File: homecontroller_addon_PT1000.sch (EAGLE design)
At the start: 46 parts, among them U1 OPA2188AIDGKR, U2 OPA2188AIDGKR, U3 REF3025AIDBZTG4, U4 ADS1015IDGST, X1 S2L3.50/10/90G

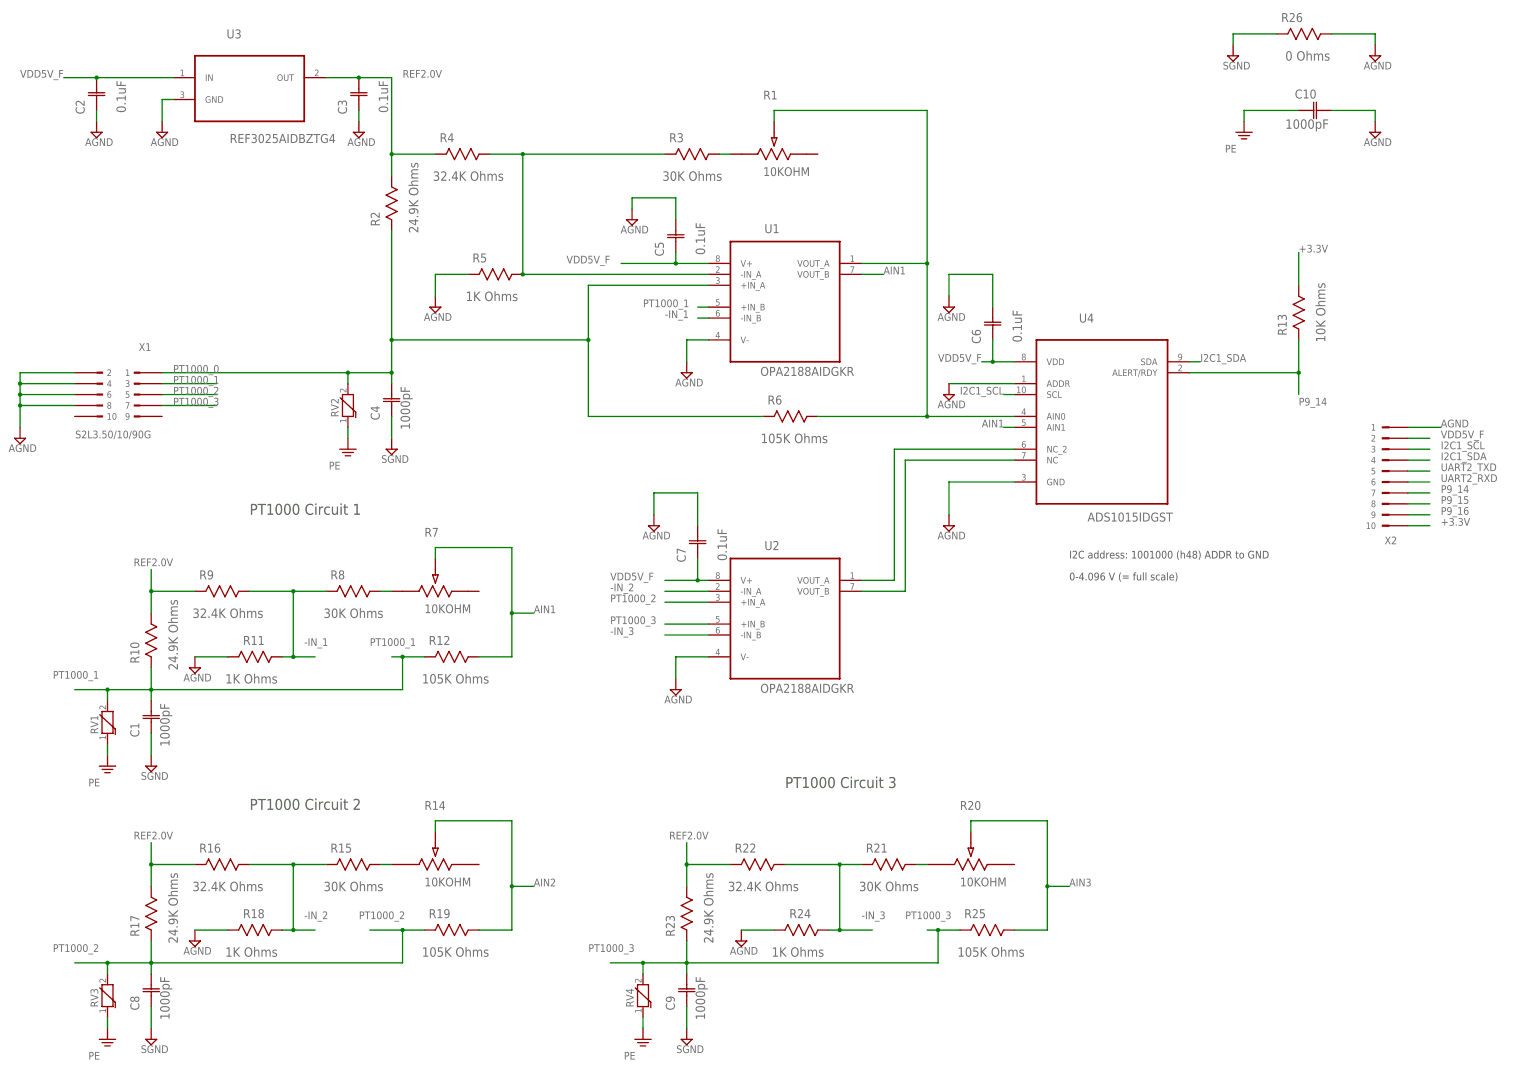
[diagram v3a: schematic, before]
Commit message: optimisation of BOM
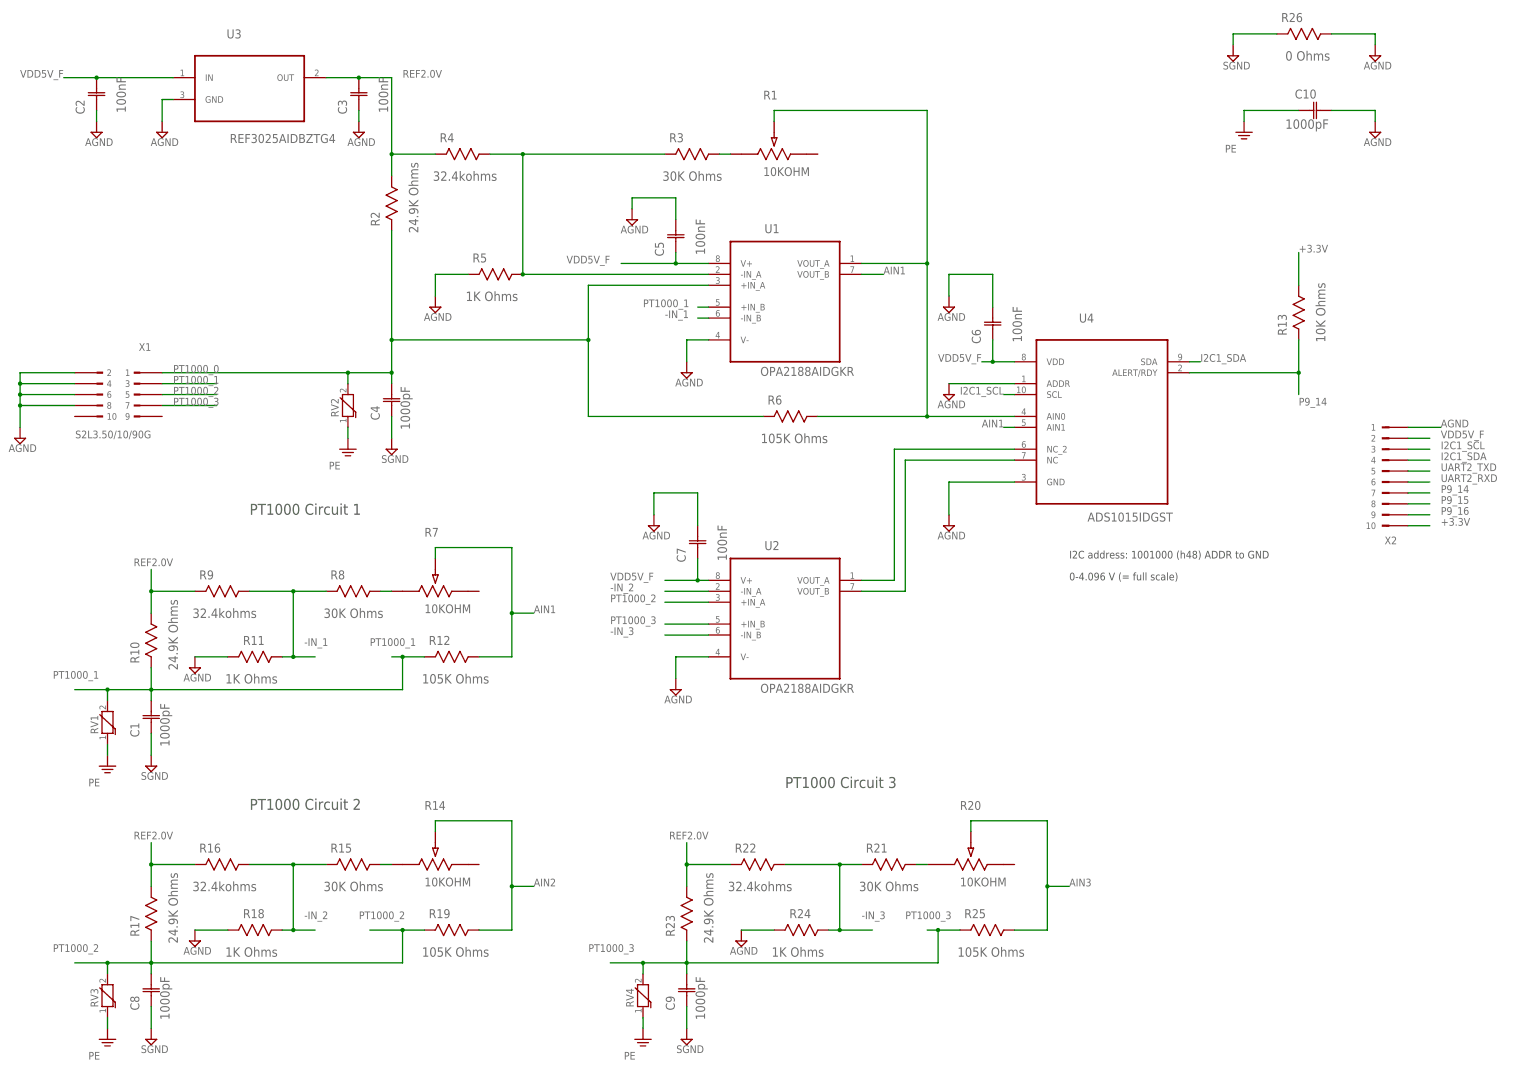
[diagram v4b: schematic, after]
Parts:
- C2, C3, C5, C6, C7: value 0.1uF -> 100nF; device Kemet_By_element14_1:C0805F104K5RACAUTO -> Kemet_By_element14_1:C0805C104K5RACTU
- R16, R22, R4, R9: value 32.4K Ohms -> 32.4kohms; device Vishay_By_element14_Batch_1:CRCW080532K4FKEA -> Vishay_By_element14_Batch_1:ERJ6ENF3242V; MF (none) -> PANASONIC ELECTRONIC COMPONENTS; OC_FARNELL unknown -> (none)
- RV1, RV2, RV3, RV4: device WE-VS:WE-VS-82550140_0805 -> WE-VS:MC-VZ-MCVZ0805M180AGT_0805; MF WURTH ELEKTRONIK -> MULTICOMP
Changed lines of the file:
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@@
 <attribute name="MF" value="VISHAY DRALORIC"/>
 </part>
-<part name="R4" library="Vishay_By_element14_Batch_1" deviceset="CRCW080532K4FKEA" device="" value="32.4K Ohms">
-<attribute name="MF" value=""/>
-<attribute name="MPN" value=""/>
-<attribute name="OC_FARNELL" value="unknown"/>
+<part name="R4" library="Vishay_By_element14_Batch_1" deviceset="ERJ6ENF3242V" device="" value="32.4kohms">
+<attribute name="MF" value="PANASONIC ELECTRONIC COMPONENTS"/>
 </part>
 <part name="R5" library="Vishay_By_element14_Batch_1" deviceset="CRCW08051K00FKEA" device="" value="1K Ohms">
@@
 <attribute name="MF" value="VISHAY DRALORIC"/>
 </part>
-<part name="R9" library="Vishay_By_element14_Batch_1" deviceset="CRCW080532K4FKEA" device="" value="32.4K Ohms">
-<attribute name="MF" value=""/>
-<attribute name="MPN" value=""/>
-<attribute name="OC_FARNELL" value="unknown"/>
+<part name="R9" library="Vishay_By_element14_Batch_1" deviceset="ERJ6ENF3242V" device="" value="32.4kohms">
+<attribute name="MF" value="PANASONIC ELECTRONIC COMPONENTS"/>
 </part>
 <part name="R10" library="Vishay_By_element14_Batch_1" deviceset="CRCW080524K9FKEA" device="" value="24.9K Ohms">
@@
 <attribute name="MF" value="VISHAY DRALORIC"/>
 </part>
-<part name="RV1" library="WE-VS" deviceset="WE-VS" device="_0805" technology="-82550140">
-<attribute name="MF" value="WURTH ELEKTRONIK"/>
+<part name="RV1" library="WE-VS" deviceset="MC-VZ" device="_0805" technology="-MCVZ0805M180AGT">
+<attribute name="MF" value="MULTICOMP"/>
 </part>
 <part name="C1" library="supply2" deviceset="C1206C102KDRACTU" device="" value="1000pF">
@@
 <attribute name="OC_FARNELL" value="1826304"/>
 </part>
-<part name="C2" library="Kemet_By_element14_1" deviceset="C0805F104K5RACAUTO" device="" value="0.1uF">
+<part name="C2" library="Kemet_By_element14_1" deviceset="C0805C104K5RACTU" device="" value="100nF">
 <attribute name="MF" value="KEMET"/>
 </part>
-<part name="C3" library="Kemet_By_element14_1" deviceset="C0805F104K5RACAUTO" device="" value="0.1uF">
+<part name="C3" library="Kemet_By_element14_1" deviceset="C0805C104K5RACTU" device="" value="100nF">
 <attribute name="MF" value="KEMET"/>
 </part>
-<part name="RV2" library="WE-VS" deviceset="WE-VS" device="_0805" technology="-82550140">
-<attribute name="MF" value="WURTH ELEKTRONIK"/>
+<part name="RV2" library="WE-VS" deviceset="MC-VZ" device="_0805" technology="-MCVZ0805M180AGT">
+<attribute name="MF" value="MULTICOMP"/>
 </part>
 <part name="C4" library="supply2" deviceset="C1206C102KDRACTU" device="" value="1000pF">
@@
 </part>
 <part name="SGND" library="strasys_standard" deviceset="GND2" device="" value="SGND"/>
-<part name="C5" library="Kemet_By_element14_1" deviceset="C0805F104K5RACAUTO" device="" value="0.1uF">
+<part name="C5" library="Kemet_By_element14_1" deviceset="C0805C104K5RACTU" device="" value="100nF">
 <attribute name="MF" value="KEMET"/>
 </part>
@@
 <attribute name="MF" value="VISHAY DRALORIC"/>
 </part>
-<part name="C6" library="Kemet_By_element14_1" deviceset="C0805F104K5RACAUTO" device="" value="0.1uF">
+<part name="C6" library="Kemet_By_element14_1" deviceset="C0805C104K5RACTU" device="" value="100nF">
 <attribute name="MF" value="KEMET"/>
 </part>
-<part name="C7" library="Kemet_By_element14_1" deviceset="C0805F104K5RACAUTO" device="" value="0.1uF">
+<part name="C7" library="Kemet_By_element14_1" deviceset="C0805C104K5RACTU" device="" value="100nF">
 <attribute name="MF" value="KEMET"/>
 </part>
@@
 <attribute name="MF" value="VISHAY DRALORIC"/>
 </part>
-<part name="R16" library="Vishay_By_element14_Batch_1" deviceset="CRCW080532K4FKEA" device="" value="32.4K Ohms">
-<attribute name="MF" value=""/>
-<attribute name="MPN" value=""/>
-<attribute name="OC_FARNELL" value="unknown"/>
+<part name="R16" library="Vishay_By_element14_Batch_1" deviceset="ERJ6ENF3242V" device="" value="32.4kohms">
+<attribute name="MF" value="PANASONIC ELECTRONIC COMPONENTS"/>
 </part>
 <part name="R17" library="Vishay_By_element14_Batch_1" deviceset="CRCW080524K9FKEA" device="" value="24.9K Ohms">
@@
 <attribute name="MF" value="VISHAY DRALORIC"/>
 </part>
-<part name="RV3" library="WE-VS" deviceset="WE-VS" device="_0805" technology="-82550140">
-<attribute name="MF" value="WURTH ELEKTRONIK"/>
+<part name="RV3" library="WE-VS" deviceset="MC-VZ" device="_0805" technology="-MCVZ0805M180AGT">
+<attribute name="MF" value="MULTICOMP"/>
 </part>
 <part name="C8" library="supply2" deviceset="C1206C102KDRACTU" device="" value="1000pF">
@@
 <attribute name="MF" value="VISHAY DRALORIC"/>
 </part>
-<part name="R22" library="Vishay_By_element14_Batch_1" deviceset="CRCW080532K4FKEA" device="" value="32.4K Ohms">
-<attribute name="MF" value=""/>
-<attribute name="MPN" value=""/>
-<attribute name="OC_FARNELL" value="unknown"/>
+<part name="R22" library="Vishay_By_element14_Batch_1" deviceset="ERJ6ENF3242V" device="" value="32.4kohms">
+<attribute name="MF" value="PANASONIC ELECTRONIC COMPONENTS"/>
 </part>
 <part name="R23" library="Vishay_By_element14_Batch_1" deviceset="CRCW080524K9FKEA" device="" value="24.9K Ohms">
@@
 <attribute name="MF" value="VISHAY DRALORIC"/>
 </part>
-<part name="RV4" library="WE-VS" deviceset="WE-VS" device="_0805" technology="-82550140">
-<attribute name="MF" value="WURTH ELEKTRONIK"/>
+<part name="RV4" library="WE-VS" deviceset="MC-VZ" device="_0805" technology="-MCVZ0805M180AGT">
+<attribute name="MF" value="MULTICOMP"/>
 </part>
 <part name="C9" library="supply2" deviceset="C1206C102KDRACTU" device="" value="1000pF">

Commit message: update
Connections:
- new net REF2.5V: C3.C2, R2.1, R4.2, U3.OUT
- net REF2.0V: no longer C3.C2, R2.1, R4.2, U3.OUT
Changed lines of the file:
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@@
 <net name="REF2.0V" class="0">
-<segment>
-<pinref part="U3" gate="A" pin="OUT"/>
-<wire x1="86.36" y1="233.68" x2="93.98" y2="233.68" width="0.1524" layer="91"/>
-<label x="104.14" y="233.68" size="1.778" layer="95"/>
-<wire x1="93.98" y1="233.68" x2="101.6" y2="233.68" width="0.1524" layer="91"/>
-<wire x1="101.6" y1="233.68" x2="101.6" y2="215.9" width="0.1524" layer="91"/>
-<pinref part="R2" gate="A" pin="1"/>
-<wire x1="101.6" y1="210.82" x2="101.6" y2="215.9" width="0.1524" layer="91"/>
-<pinref part="R4" gate="A" pin="2"/>
-<wire x1="111.76" y1="215.9" x2="101.6" y2="215.9" width="0.1524" layer="91"/>
-<junction x="101.6" y="215.9"/>
-<pinref part="C3" gate="A" pin="C2"/>
-<junction x="93.98" y="233.68"/>
-</segment>
 <segment>
 <wire x1="45.72" y1="119.38" x2="45.72" y2="114.3" width="0.1524" layer="91"/>
@@
 </segment>
 </net>
+<net name="REF2.5V" class="0">
+<segment>
+<pinref part="U3" gate="A" pin="OUT"/>
+<wire x1="86.36" y1="233.68" x2="93.98" y2="233.68" width="0.1524" layer="91"/>
+<label x="104.14" y="233.68" size="1.778" layer="95"/>
+<wire x1="93.98" y1="233.68" x2="101.6" y2="233.68" width="0.1524" layer="91"/>
+<wire x1="101.6" y1="233.68" x2="101.6" y2="215.9" width="0.1524" layer="91"/>
+<pinref part="R2" gate="A" pin="1"/>
+<wire x1="101.6" y1="210.82" x2="101.6" y2="215.9" width="0.1524" layer="91"/>
+<pinref part="R4" gate="A" pin="2"/>
+<wire x1="111.76" y1="215.9" x2="101.6" y2="215.9" width="0.1524" layer="91"/>
+<junction x="101.6" y="215.9"/>
+<pinref part="C3" gate="A" pin="C2"/>
+<junction x="93.98" y="233.68"/>
+</segment>
+</net>

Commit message: PT1000 update
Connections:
- removed net REF2.0V: R10.1, R16.2, R17.1, R22.2, R23.1, R9.2
- net REF2.5V: now also R10.1, R16.2, R17.1, R22.2, R23.1, R9.2
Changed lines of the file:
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@@
-</segment>
-</net>
-<net name="REF2.0V" class="0">
-<segment>
-<wire x1="45.72" y1="119.38" x2="45.72" y2="114.3" width="0.1524" layer="91"/>
-<wire x1="45.72" y1="109.22" x2="45.72" y2="114.3" width="0.1524" layer="91"/>
-<pinref part="R9" gate="A" pin="2"/>
-<wire x1="55.88" y1="114.3" x2="45.72" y2="114.3" width="0.1524" layer="91"/>
-<junction x="45.72" y="114.3"/>
-<pinref part="R10" gate="A" pin="1"/>
-<label x="50.8" y="121.92" size="1.778" layer="95" rot="R180"/>
-</segment>
-<segment>
-<wire x1="45.72" y1="55.88" x2="45.72" y2="50.8" width="0.1524" layer="91"/>
-<wire x1="45.72" y1="45.72" x2="45.72" y2="50.8" width="0.1524" layer="91"/>
-<pinref part="R16" gate="A" pin="2"/>
-<wire x1="55.88" y1="50.8" x2="45.72" y2="50.8" width="0.1524" layer="91"/>
-<junction x="45.72" y="50.8"/>
-<pinref part="R17" gate="A" pin="1"/>
-<label x="50.8" y="58.42" size="1.778" layer="95" rot="R180"/>
-</segment>
-<segment>
-<wire x1="170.18" y1="55.88" x2="170.18" y2="50.8" width="0.1524" layer="91"/>
-<wire x1="170.18" y1="45.72" x2="170.18" y2="50.8" width="0.1524" layer="91"/>
-<pinref part="R22" gate="A" pin="2"/>
-<wire x1="180.34" y1="50.8" x2="170.18" y2="50.8" width="0.1524" layer="91"/>
-<junction x="170.18" y="50.8"/>
-<pinref part="R23" gate="A" pin="1"/>
-<label x="175.26" y="58.42" size="1.778" layer="95" rot="R180"/>
 </segment>
 </net>
@@
 <junction x="93.98" y="233.68"/>
 </segment>
-</net>
+<segment>
+<wire x1="45.72" y1="119.38" x2="45.72" y2="114.3" width="0.1524" layer="91"/>
+<wire x1="45.72" y1="109.22" x2="45.72" y2="114.3" width="0.1524" layer="91"/>
+<pinref part="R9" gate="A" pin="2"/>
+<wire x1="55.88" y1="114.3" x2="45.72" y2="114.3" width="0.1524" layer="91"/>
+<junction x="45.72" y="114.3"/>
+<pinref part="R10" gate="A" pin="1"/>
+<label x="50.8" y="121.92" size="1.778" layer="95" rot="R180"/>
+</segment>
+<segment>
+<wire x1="45.72" y1="55.88" x2="45.72" y2="50.8" width="0.1524" layer="91"/>
+<wire x1="45.72" y1="45.72" x2="45.72" y2="50.8" width="0.1524" layer="91"/>
+<pinref part="R16" gate="A" pin="2"/>
+<wire x1="55.88" y1="50.8" x2="45.72" y2="50.8" width="0.1524" layer="91"/>
+<junction x="45.72" y="50.8"/>
+<pinref part="R17" gate="A" pin="1"/>
+<label x="50.8" y="58.42" size="1.778" layer="95" rot="R180"/>
+</segment>
+<segment>
+<wire x1="170.18" y1="55.88" x2="170.18" y2="50.8" width="0.1524" layer="91"/>
+<wire x1="170.18" y1="45.72" x2="170.18" y2="50.8" width="0.1524" layer="91"/>
+<pinref part="R22" gate="A" pin="2"/>
+<wire x1="180.34" y1="50.8" x2="170.18" y2="50.8" width="0.1524" layer="91"/>
+<junction x="170.18" y="50.8"/>
+<pinref part="R23" gate="A" pin="1"/>
+<label x="175.26" y="58.42" size="1.778" layer="95" rot="R180"/>
+</segment>
+</net>

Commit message: update PT1000
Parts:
- added R27, R28: 4.7K Ohms, Vishay_By_element14_Batch_1:CRCW08054K70FKEA
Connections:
- net +3.3V: now also R27.1, R28.1
- net I2C1_SCL: now also R28.2
- net I2C1_SDA: now also R27.2
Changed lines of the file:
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@@
 <attribute name="OC_FARNELL" value="unknown"/>
 </part>
+<part name="R27" library="Vishay_By_element14_Batch_1" deviceset="CRCW08054K70FKEA" device="" value="4.7K Ohms"/>
+<part name="R28" library="Vishay_By_element14_Batch_1" deviceset="CRCW08054K70FKEA" device="" value="4.7K Ohms"/>
 </parts>
 <sheets>
@@
 <attribute name="MPN" x="337.82" y="152.4" size="1.778" layer="96" display="off"/>
 </instance>
+<instance part="R27" gate="A" x="312.42" y="81.28" smashed="yes" rot="R90">
+<attribute name="VALUE" x="316.0776" y="80.6958" size="1.778" layer="96" rot="SR90"/>
+<attribute name="NAME" x="309.6514" y="82.2706" size="2.0828" layer="95" ratio="10" rot="SR90"/>
+</instance>
+<instance part="R28" gate="A" x="325.12" y="81.28" smashed="yes" rot="R90">
+<attribute name="VALUE" x="328.7776" y="80.6958" size="1.778" layer="96" rot="SR90"/>
+<attribute name="NAME" x="322.3514" y="82.2706" size="2.0828" layer="95" ratio="10" rot="SR90"/>
+</instance>
 </instances>
 <busses>
@@
 <label x="312.42" y="193.04" size="1.778" layer="95"/>
 </segment>
+<segment>
+<wire x1="325.12" y1="93.98" x2="325.12" y2="104.14" width="0.1524" layer="91"/>
+<wire x1="325.12" y1="104.14" x2="342.9" y2="104.14" width="0.1524" layer="91"/>
+<pinref part="R28" gate="A" pin="1"/>
+<wire x1="312.42" y1="93.98" x2="312.42" y2="104.14" width="0.1524" layer="91"/>
+<wire x1="312.42" y1="104.14" x2="325.12" y2="104.14" width="0.1524" layer="91"/>
+<pinref part="R27" gate="A" pin="1"/>
+<junction x="325.12" y="104.14"/>
+</segment>
 </net>
 <net name="P9_16" class="0">
@@
 <label x="233.68" y="160.02" size="1.778" layer="95"/>
 <pinref part="U4" gate="A" pin="SCL"/>
+</segment>
+<segment>
+<wire x1="304.8" y1="73.66" x2="325.12" y2="73.66" width="0.1524" layer="91"/>
+<wire x1="325.12" y1="73.66" x2="350.52" y2="73.66" width="0.1524" layer="91"/>
+<wire x1="325.12" y1="81.28" x2="325.12" y2="73.66" width="0.1524" layer="91"/>
+<junction x="325.12" y="73.66"/>
+<label x="353.06" y="73.66" size="1.778" layer="95"/>
+<pinref part="R28" gate="A" pin="2"/>
 </segment>
 </net>
@@
 <pinref part="X2" gate="G$1" pin="4"/>
 </segment>
-</net>
+<segment>
+<wire x1="350.52" y1="68.58" x2="312.42" y2="68.58" width="0.1524" layer="91"/>
+<wire x1="312.42" y1="68.58" x2="304.8" y2="68.58" width="0.1524" layer="91"/>
+<wire x1="312.42" y1="81.28" x2="312.42" y2="68.58" width="0.1524" layer="91"/>
+<junction x="312.42" y="68.58"/>
+<label x="353.06" y="68.58" size="1.778" layer="95"/>
+<pinref part="R27" gate="A" pin="2"/>
+</segment>
+</net>
